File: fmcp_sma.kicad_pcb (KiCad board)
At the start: 4 copper layers, 78.5 x 69 mm, 40 parts, among them J101 Conn_Coaxial, J102 Conn_Coaxial, J103 FMCP_VITA57.4, J104 Conn_Coaxial, J105 Conn_Coaxial, J106 Conn_Coaxial, J107 Conn_Coaxial, J108 Conn_Coaxial, J109 Conn_Coaxial, J110 Conn_Coaxial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

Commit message: images
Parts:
- C118, R110, R111, U101: moved to B.Cu
- moved R110 3.92 mm to (171.9, 49.0)
- moved R111 3.45 mm to (171.9, 51.0)
- moved C118 2.24 mm to (171.9, 53.0)
- moved U101 2.24 mm to (164.9, 51.0)
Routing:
- net (no net): track 0.00 -> 16.2 mm, vias 37 -> 61
- net Net-(J103-PadB28): track 0.90 -> 0.00 mm, vias 1 -> 0
- net Net-(J103-PadB24): track 0.90 -> 0.00 mm, vias 1 -> 0
- net Net-(J103-PadA38): track 0.90 -> 0.00 mm, vias 2 -> 0
- net Net-(J103-PadA31): track 0.90 -> 0.00 mm, vias 2 -> 0
- net Net-(J103-PadA27): track 0.90 -> 0.00 mm, vias 1 -> 0
- net Net-(J103-PadA14): track 0.90 -> 0.00 mm, vias 1 -> 0
- net Net-(J103-PadA10): track 0.90 -> 0.00 mm, vias 1 -> 0
- net Net-(J103-PadA39): track 0.90 -> 0.00 mm, vias 2 -> 0
- net Net-(J103-PadA35): track 0.90 -> 0.00 mm, vias 2 -> 0
- net Net-(J103-PadA34): track 0.90 -> 0.00 mm, vias 2 -> 0
- net Net-(J103-PadA30): track 0.90 -> 0.00 mm, vias 2 -> 0
- net Net-(J103-PadB29): track 0.90 -> 0.00 mm, vias 1 -> 0
- net Net-(J103-PadB25): track 0.90 -> 0.00 mm, vias 1 -> 0
- net Net-(J103-PadA26): track 0.90 -> 0.00 mm, vias 1 -> 0
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
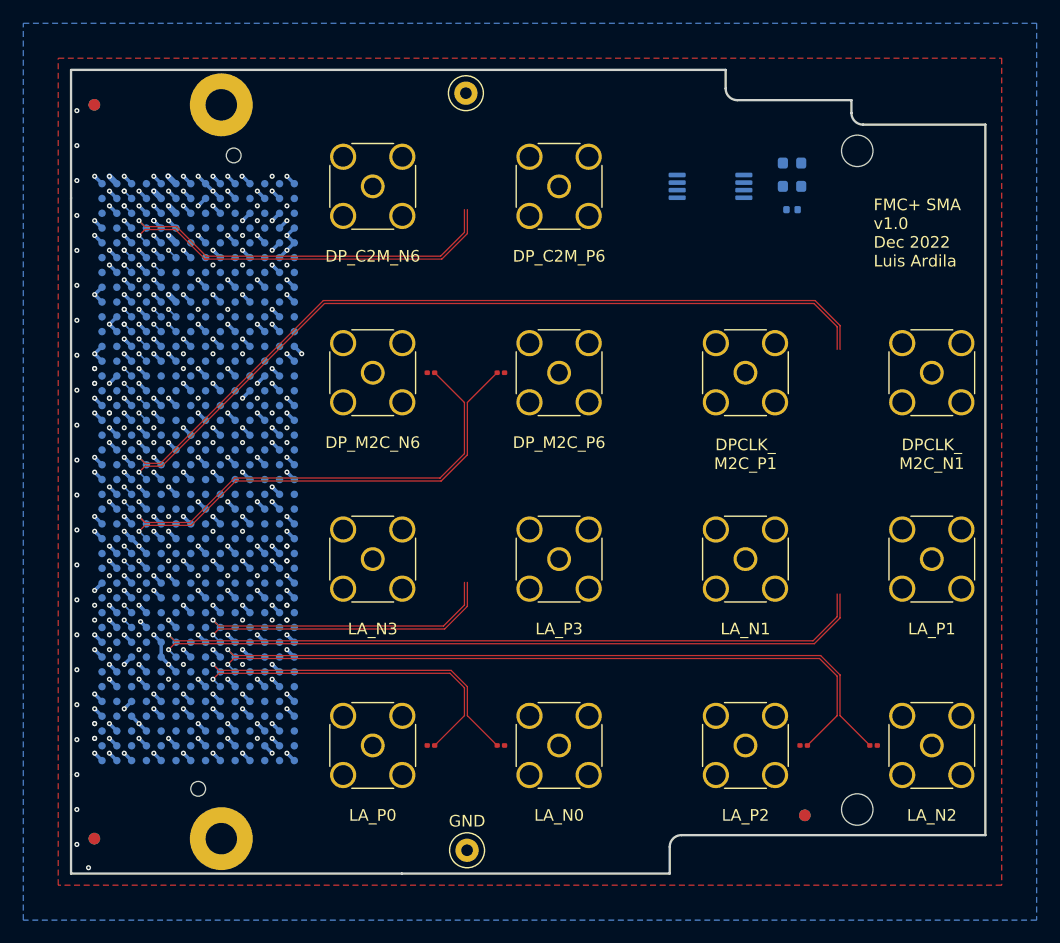
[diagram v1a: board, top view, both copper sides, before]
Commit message: updated footprint
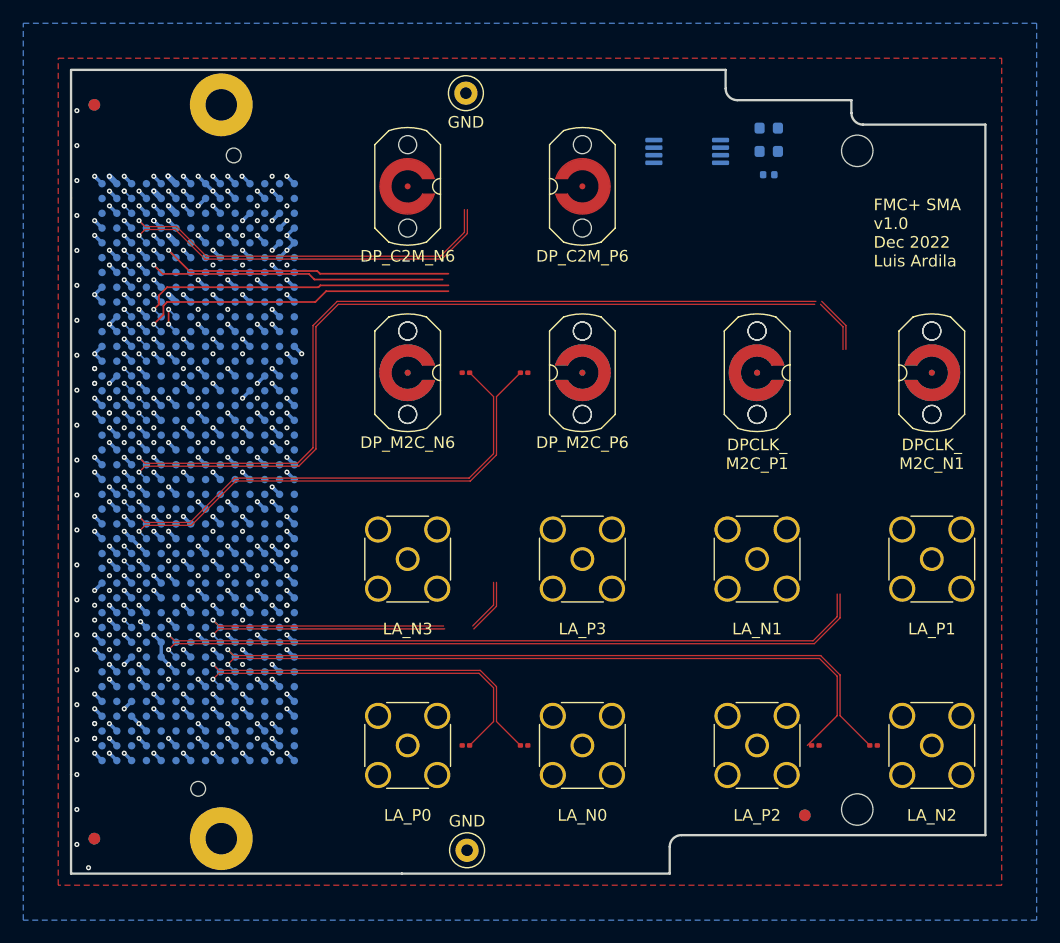
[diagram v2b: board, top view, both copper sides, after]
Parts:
- added J116: Conn_Coaxial, KIT_Connector:SF2921-61345-1S, B.Cu at (168.9, 67.0)
- added J117: Conn_Coaxial, KIT_Connector:SF2921-61345-1S, B.Cu at (183.9, 67.0)
- added J118: Conn_Coaxial, KIT_Connector:SF2921-61345-1S, B.Cu at (153.9, 67.0)
- added J119: Conn_Coaxial, KIT_Connector:SF2921-61345-1S, B.Cu at (138.9, 67.0)
- J101, J102, J104, J105, J106, J107: footprint Connector_Coaxial:SMA_Amphenol_132134_Vertical -> KIT_Connector:SF2921-61345-1S
- moved C118 3.61 mm to (169.9, 50.0)
- moved R110 3.61 mm to (169.9, 46.0)
- moved R111 3.61 mm to (169.9, 48.0)
- moved U101 3.61 mm to (162.9, 48.0)
- moved C102 3.00 mm to (143.9, 67.0)
- moved C103 3.00 mm to (143.9, 99.0)
- moved J102 3.00 mm to (138.9, 51.0)
- moved J107 3.00 mm to (138.9, 67.0)
- moved J110 3.00 mm to (138.9, 99.0)
- moved J115 3.00 mm to (138.9, 83.0)
- moved C101 2.00 mm to (148.9, 67.0)
- moved C104 2.00 mm to (148.9, 99.0)
- moved J101 2.00 mm to (153.9, 51.0), turned to 0 degrees
- moved J106 2.00 mm to (153.9, 67.0), turned to 0 degrees
- moved J111 2.00 mm to (153.9, 99.0)
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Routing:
- net /SCL: track 0.90 -> 27.8 mm
- net /SDA: track 0.90 -> 27.5 mm
- net /GA0: track 0.90 -> 26.2 mm
- net /GA1: track 0.90 -> 25.8 mm
- net /DPCLK_M2C_P1: track 69.6 -> 75.7 mm
- net /DPCLK_M2C_N1: track 70.0 -> 76.1 mm
- net /DP_M2C_C_N6: track 39.5 -> 41.8 mm
- net /LA_C_P0: track 29.2 -> 31.5 mm
- net /LA_C_N0: track 29.6 -> 31.9 mm
- net /DP_M2C_C_P6: track 39.9 -> 42.2 mm
- net Net-(J103-PadD30): track 1.80 -> 3.07 mm

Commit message: routed
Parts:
- added C107: 0.1uF, Capacitor_SMD:C_0201_0603Metric, B.Cu at (175.7, 67.0)
- added C108: 0.1uF, Capacitor_SMD:C_0201_0603Metric, B.Cu at (177.2, 67.0)
- added C109: 1uF, Capacitor_SMD:C_0603_1608Metric, B.Cu at (171.4, 50.5)
- added R101: 0, Resistor_SMD:R_0201_0603Metric, F.Cu at (147.2, 83.0)
- added R102: 0, Resistor_SMD:R_0201_0603Metric, F.Cu at (145.7, 83.0)
- added R103: 0, Resistor_SMD:R_0201_0603Metric, F.Cu at (147.2, 67.0)
- added R104: 0, Resistor_SMD:R_0201_0603Metric, F.Cu at (145.7, 67.0)
- added R105: 0, Resistor_SMD:R_0201_0603Metric, F.Cu at (177.2, 83.0)
- added R106: 0, Resistor_SMD:R_0201_0603Metric, F.Cu at (175.7, 83.0)
- added R107: 0, Resistor_SMD:R_0201_0603Metric, F.Cu at (147.2, 51.0)
- added R108: 0, Resistor_SMD:R_0201_0603Metric, F.Cu at (145.7, 51.0)
- added R109: 0, Resistor_SMD:R_0201_0603Metric, B.Cu at (147.2, 67.0)
- added R112: 0, Resistor_SMD:R_0201_0603Metric, B.Cu at (145.7, 67.0)
- C118: footprint Capacitor_SMD:C_0402_1005Metric -> Capacitor_SMD:C_0603_1608Metric
- moved J105 45.0 mm to (138.9, 67.0), turned to 180 degrees
- moved C102 31.8 mm to (175.7, 67.0)
- moved J106 30.0 mm to (183.9, 67.0)
- moved J107 30.0 mm to (168.9, 67.0)
- moved J117 30.0 mm to (153.9, 67.0)
- moved J118 30.0 mm to (183.9, 67.0)
- moved C101 28.2 mm to (177.2, 67.0)
- moved J104 15.0 mm to (153.9, 67.0), turned to 0 degrees
- moved U101 2.06 mm to (164.9, 47.5)
- moved C118 1.80 mm to (171.4, 49.0)
- moved C103 1.75 mm to (145.7, 99.0)
- moved C104 1.75 mm to (147.2, 99.0)
- moved C105 1.75 mm to (175.7, 99.0)
- moved C106 1.75 mm to (177.2, 99.0)
- moved R111 1.58 mm to (171.4, 47.5)
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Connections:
- J103 pad B20: /DPCLK_M2C_P1 -> /DPCLK_M2C_R_P1
- J103 pad B21: /DPCLK_M2C_N1 -> /DPCLK_M2C_R_N1
- J103 pad B36: /DP_C2M_P6 -> /DP_C2M_R_P6
- J103 pad B37: /DP_C2M_N6 -> /DP_C2M_R_N6
- J103 pad D8: /LA_P1 -> /LA_R_P1
- J103 pad D9: /LA_N1 -> /LA_R_N1
- J103 pad G10: /LA_N3 -> /LA_R_N3
- J103 pad G9: /LA_P3 -> /LA_R_P3
- J116 pad 1: /Test_100_Ohm_P -> Net-(C107-Pad1)
- J117 pad 1: /Test_100_Ohm_P -> Net-(J117-Pad1)
- J118 pad 1: /Test_100_Ohm_N -> Net-(C108-Pad1)
- J119 pad 1: /Test_100_Ohm_N -> Net-(J119-Pad1)
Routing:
- net /DPCLK_M2C_N1: track 76.1 -> 6.43 mm, vias 1 -> 0
- net /DPCLK_M2C_P1: track 75.7 -> 6.43 mm, vias 1 -> 0
- net /LA_R_P1: track 0.00 -> 65.9 mm, vias 0 -> 1
- net /LA_R_N1: track 0.00 -> 65.5 mm, vias 0 -> 1
- net /LA_P1: track 61.7 -> 6.43 mm, vias 1 -> 0
- net /LA_N1: track 61.3 -> 6.43 mm, vias 1 -> 0
- net /Test_100_Ohm_N: track 0.00 -> 44.4 mm
- net /Test_100_Ohm_P: track 0.00 -> 43.6 mm
- net /SCL: track 27.8 -> 70.8 mm, vias 1 -> 2
- net /SDA: track 27.5 -> 70.0 mm, vias 1 -> 2
- net /DPCLK_M2C_R_P1: track 0.00 -> 39.1 mm, vias 0 -> 1
- net /DPCLK_M2C_R_N1: track 0.00 -> 38.7 mm, vias 0 -> 1
- net /DP_C2M_R_P6: track 0.00 -> 38.1 mm, vias 0 -> 1
- net /DP_C2M_R_N6: track 0.00 -> 37.7 mm, vias 0 -> 1
- net /GA0: track 26.2 -> 57.4 mm, vias 1 -> 2
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- added copper zone on In2_GND.Cu, net GND
- removed copper zone on In2.Cu, net GND
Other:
- net class microstrip: clearance 0.1 -> 0.115; trace_width 0.15 -> 0.12
- net class stripline removed

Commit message: gerbers
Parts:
- added R113: 4.7k, Resistor_SMD:R_0603_1608Metric, B.Cu at (117.1, 43.1)
- moved G101 6.65 mm to (184.2, 54.4), turned to 90 degrees
- moved G102 2.68 mm to (183.2, 58.4), turned to 90 degrees
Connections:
- J103 pad F1: (no net) -> /PG_M2C
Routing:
- net +3V3_FMCP: track 13.4 -> 89.1 mm
- net /PG_M2C: track 0.00 -> 70.5 mm, vias 0 -> 2
- net (no net): track 16.2 -> 0.00 mm, vias 61 -> 4
- net GND: track 222.3 -> 226.6 mm
- net +12V_FMCP: track 4.49 -> 8.83 mm
- net +1V8_FMCP: track 4.49 -> 8.08 mm

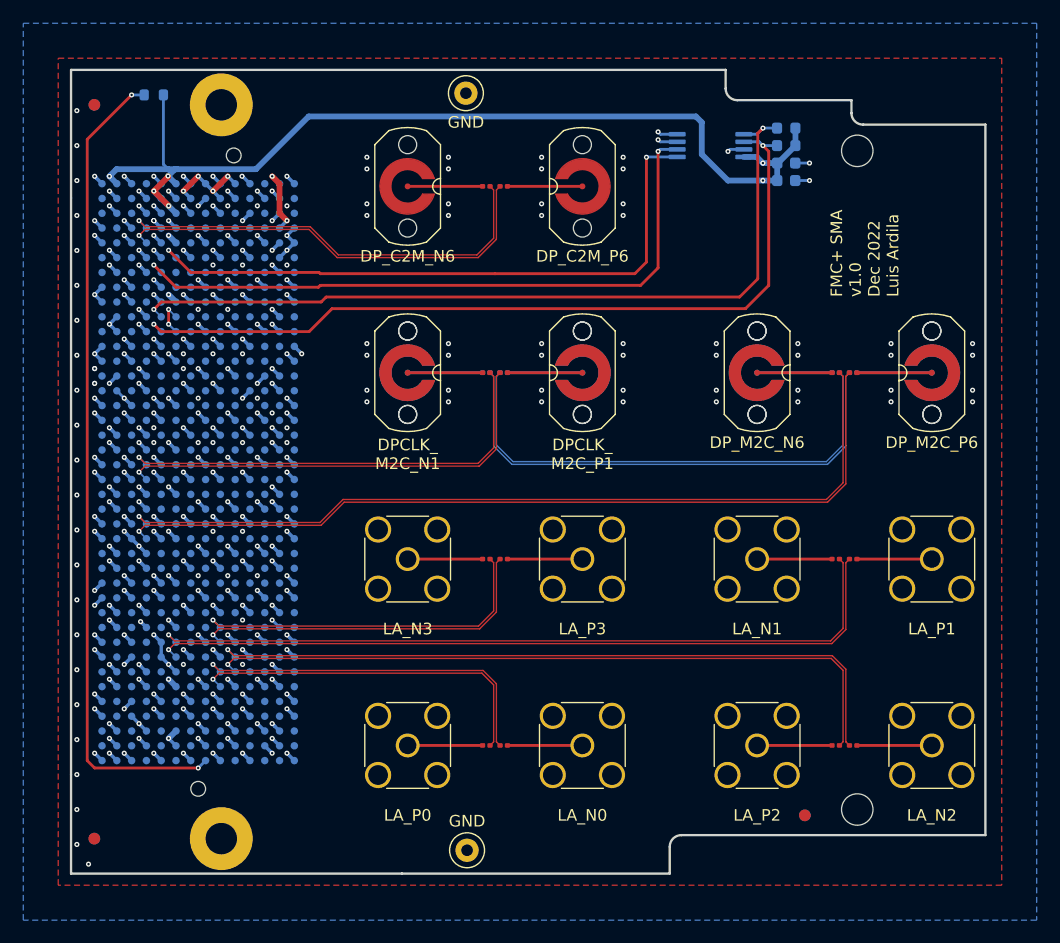
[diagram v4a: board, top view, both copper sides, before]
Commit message: modified footprint for screw on sma conn@
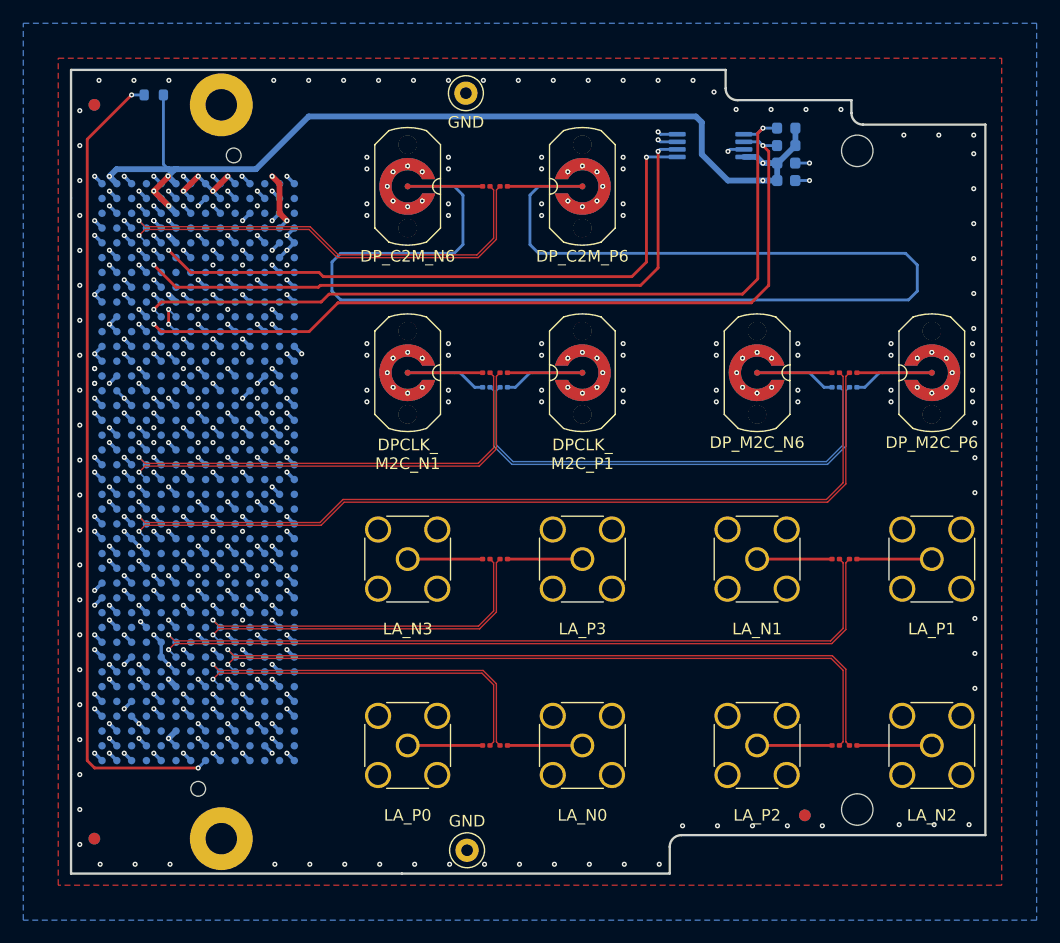
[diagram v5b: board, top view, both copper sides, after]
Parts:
- added G***: LOGO, KIT_Graphic:IPE_LOGO_MASK_2.5x1.4mm, F.Cu at (180.7, 59.2)
- added J120: Conn_Coaxial, KIT_Connector:SF2921-61345-1S, B.Cu at (138.9, 51.0)
- added J121: Conn_Coaxial, KIT_Connector:SF2921-61345-1S, B.Cu at (153.9, 51.0)
- moved G102 6.70 mm to (176.5, 59.2), turned to 0 degrees
- moved G101 5.86 mm to (184.4, 60.2), turned to 0 degrees
- moved C107 1.25 mm to (175.7, 68.2)
- moved C108 1.25 mm to (177.2, 68.2)
- moved R109 1.25 mm to (147.2, 68.2)
- moved R112 1.25 mm to (145.7, 68.2)
- turned J110 to 90 degrees
- turned J111 to 90 degrees
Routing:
- net /Test_50_Ohm: track 0.00 -> 119.8 mm
- net /Test_100_Ohm_N: track 44.4 -> 41.9 mm
- net /Test_100_Ohm_P: track 43.6 -> 41.1 mm
- net Net-(J119-Pad1): track 6.43 -> 6.95 mm
- net Net-(J117-Pad1): track 6.43 -> 6.95 mm
- net Net-(C108-Pad1): track 6.43 -> 6.95 mm
- net Net-(C107-Pad1): track 6.43 -> 6.95 mm
- net GND: vias 336 -> 436
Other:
- board text added: "FMC+ SMA v1.0 Dec 2022"
- board text added: "Luis Ardila Marvin Fuchs Robert Gartmann Lukas Scheller"
- board text removed: "FMC+ SMA v1.0 Dec 2022 Luis Ardila"

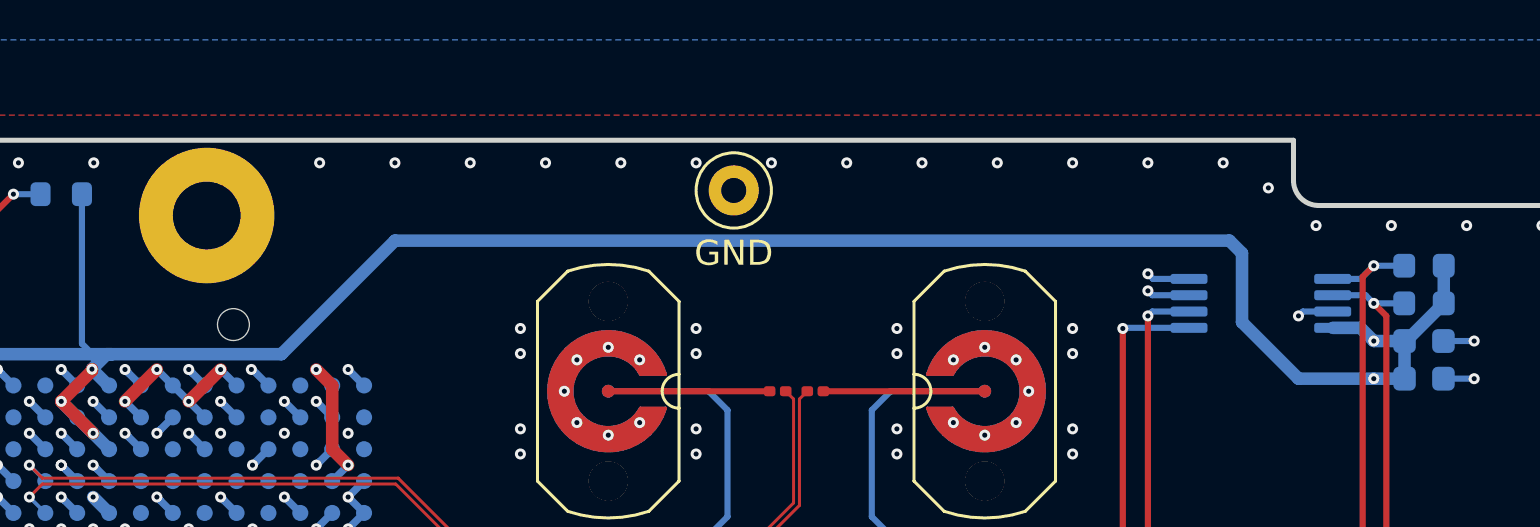
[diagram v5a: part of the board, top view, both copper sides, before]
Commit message: re-pour zones with 0.3 clearance and 1mm for traces only
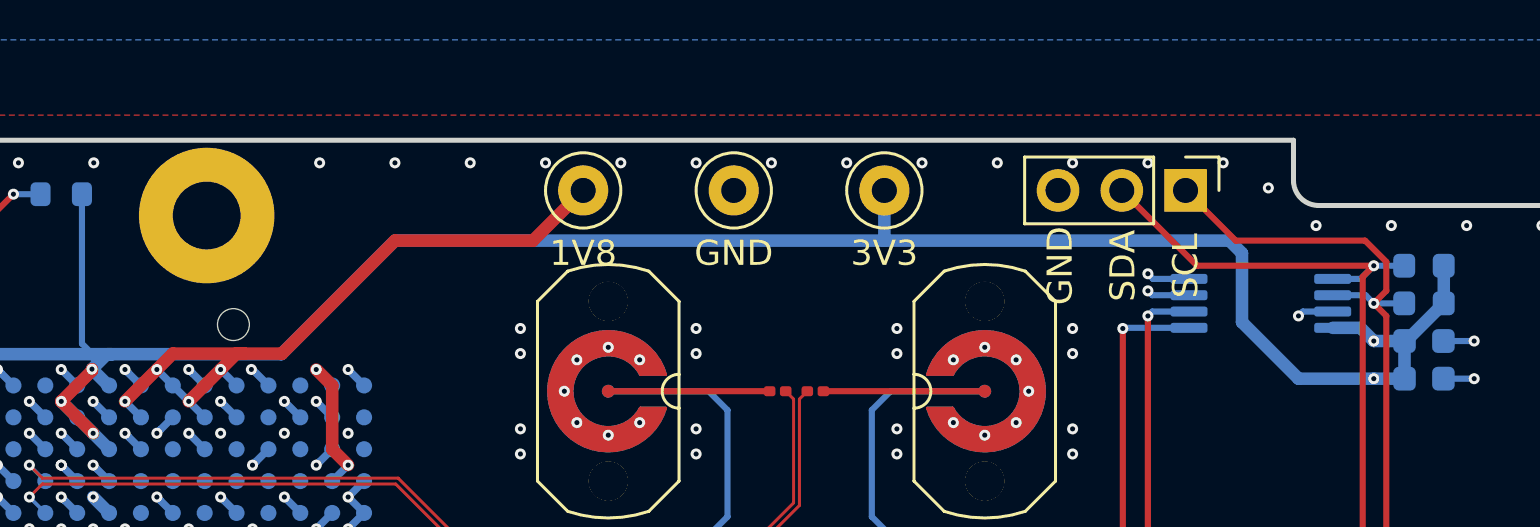
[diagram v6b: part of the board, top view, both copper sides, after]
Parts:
- added J122: Conn_01x03_Male, Connector_PinHeader_2.54mm:PinHeader_1x03_P2.54mm_Vertical, F.Cu at (161.9, 43.0)
- added TP101: TestPoint, TestPoint:TestPoint_Loop_D2.50mm_Drill1.0mm, F.Cu at (149.9, 43.0)
- added TP102: TestPoint, TestPoint:TestPoint_Loop_D2.50mm_Drill1.0mm, F.Cu at (137.9, 43.0)
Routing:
- net +1V8_FMCP: track 8.08 -> 29.2 mm
- net /SDA: track 70.0 -> 81.3 mm
- net /SCL: track 70.8 -> 81.8 mm
- net +3V3_FMCP: track 89.1 -> 91.1 mm
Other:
- board text added: "1V8"
- board text added: "3V3"
- board text added: "SCL"
- board text added: "SDA"

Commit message: updated gerbers
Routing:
- net GND: vias 436 -> 435
